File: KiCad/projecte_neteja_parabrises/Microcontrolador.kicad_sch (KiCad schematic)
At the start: 11 parts, among them J1 Conn_01x09_Pin, U1 PIC24HJ32GP302, U2 SN74LVC2T45DCUR, U3 HDC2080, Y1 Crystal

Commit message: SCH V1
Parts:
- added C1, C2: 100n, symbol Device:C
- added J2: DE9_Pins, symbol Connector:DE9_Pins
- added U1: TJA1049TK-3, Package_SON:HVSON-8-1EP_3x3mm_P0.65mm_EP1.6x2.4mm, symbol Interface_CAN_LIN:TJA1049TK-3
- J1: value Conn_01x09_Pin -> USART
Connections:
- net GATE B1 is gone; now on net SW2: U1.7 (RB3)
- net GATE B2 is gone; now on net SW3: U1.11 (RB4)
- net GATE C: now also U1.3 (RA1); no longer U1.14 (RB5)
- net GND: now also J1.4 (Pin_4), C1.2, C2.1, J2.3, U1.2 (GND), U1.9 (GND)
- net RX: now also J1.1 (Pin_1)
- net SW1: now also U1.6 (RB2); no longer U1.4 (RB0)
- net SW2: no longer U1.5 (RB1)
- net SW3: no longer U1.6 (RB2)
- net TX: now also J1.2 (Pin_2)
- net VDD: now also J1.3 (Pin_3), J2.9, U1.3 (VCC), U1.5 (VIO)
- net at U1.19 (VSS): now also C1.1
- net GATE B: now reaches U1.2 (RA0)
- net DRDY: now reaches U1.21 (RB10)
- net DRDY: now also U3.4 (DRDY)
- net CANTX: now reaches U1.22 (RP11)
- net CANTX: now also U1.1 (TXD)
- net CANRX: now reaches U1.23 (RP12)
- net CANRX: now also U1.4 (RXD)
- net at U1.8 (VSS): now also C2.2
- net RB6 renamed SW5
- net SW5: no longer U3.4 (DRDY)
- new net: J2.2, U1.6 (CANL)
- new net: J2.7, U1.7 (CANH)
- new net SW4: U1.14 (RB5)
- new net SWB: U1.5 (RB1)
- new net SWC: U1.4 (RB0)
- no-connect marks 0 -> 15
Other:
- note added: "OSCILADOR"
- note added: "SENSOR DE LLUVIA"
- note added: "USART Y BUS CAN"
- moved on the sheet: C1, C2, J1, R1, R2, R3, R4, U1, U2, U3, Y1

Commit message: UART ACABADO
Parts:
- removed J1: USART, symbol Connector:Conn_01x09_Pin
- added C5, C6, C7, C8: C, symbol Device:C
- added J3: DE9_Pins, symbol Connector:DE9_Pins
- added U7: MAX232, symbol Interface_UART:MAX232
- renumbered C1 to C3, C2 to C4, R2 to R5, R1 to R6, R3 to R7, R4 to R8, U1 to U4, U3 to U5, U2 to U6
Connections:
- net GND: now also J2.5, C7.1, C8.1, J3.5, U7.15 (GND); no longer J2.3
- net RX: now also U7.12 (R1OUT)
- net TX: now also U7.11 (T1IN)
- new net: J3.2, U7.14 (T1OUT)
- new net: J3.3, U7.13 (R1IN)
- new net: C8.2, U7.2 (VS+)
- new net: C5.1, U7.1 (C1+)
- new net: C5.2, U7.3 (C1-)
- new net: C6.1, U7.4 (C2+)
- new net: C6.2, U7.5 (C2-)
- new net: C7.2, U7.6 (VS-)
- new net VCC: U7.16 (VCC)
- no-connect marks 15 -> 22
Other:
- moved on the sheet: C1, C2, J2, U1, U4

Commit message: MICRO ACTUALIZADA
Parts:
- added C3: 100n, symbol Device:C
- added R5, R6: R, symbol Device:R
- renumbered C3 to C1, C4 to C2, C8 to C?, C6 to C?, C5 to C?, C1 to C?, C7 to C?, C2 to C?, J2 to J?, J3 to J?, R6 to R1, R5 to R2, R7 to R3, R8 to R4, U4 to U1, U6 to U2, U5 to U3, U7 to U?, U1 to U?
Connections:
- net GND: now also C3.1
- net VDD: now also R6.2
- net MCLR: now reaches U1.1 (~{MCLR})
- net MCLR: now also R5.2
- net FC1: now reaches U1.12 (RA4)
- new net: C3.2, R5.1, R6.1
- no-connect marks 22 -> 20

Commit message: ESQUEMATICO V2
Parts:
- removed C? (x4): C, symbol Device:C
- removed J? (x2): DE9_Pins, symbol Connector:DE9_Pins
- removed U?: MAX232, symbol Interface_UART:MAX232
- removed U?: TJA1049TK-3, Package_SON:HVSON-8-1EP_3x3mm_P0.65mm_EP1.6x2.4mm, symbol Interface_CAN_LIN:TJA1049TK-3
- added C17: 10p, symbol Device:C
- C3: renamed from C1; value C -> 20p
- C4: renamed from C2; value C -> 20p
- R1: renamed from R5; value R -> 470
- R2: renamed from R6; value R -> 10K
- gave numbers to parts that had none: 2
- renumbered C3 to C16, R2 to R5, R1 to R6, R3 to R7, R4 to R8, U1 to U4, U3 to U5, U2 to U6
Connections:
- net GND: now also U4.19 (VSS), U4.27 (AVSS), C17.2
- net at C1.1: now also U4.28 (AVDD); no longer U4.19 (VSS)
- net at U4.20 (VCAP): now also C17.1
- net FC2: now reaches U4.24 (RP13)
- net DRDY: no longer names the net of U5.4 (DRDY)
- net DRDY: no longer U4.21 (RB10)
- new net PWM2: U4.21 (RB10)
- no-connect marks 20 -> 1
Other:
- note added: "MICROPROCESADOR"
- note removed: "USART Y BUS CAN"
- moved on the sheet: C1, C16, C2, R1, R2, U4

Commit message: Error de nombres solucionado
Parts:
- renumbered R6 to R10, R7 to R11, R8 to R12, R1 to R7, R2 to R8, R5 to R9, U4 to U5, U5 to U6, U6 to U7
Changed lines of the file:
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@@
 		(dnp no)
 		(fields_autoplaced yes)
-		(property "Reference" "R5"
+		(property "Reference" "R9"
 			(at 234.95 48.2599 0)
 			(effects
@@
 			(project "projecte_neteja_parabrises"
 				(path "/83fe8808-b70b-463e-9fcd-89556c9690a9/7b0ed2a6-dd0e-4fb8-9a3e-b81f5336277e"
-					(reference "R5")
+					(reference "R9")
 					(unit 1)
 				)
@@
 		(dnp no)
 		(fields_autoplaced yes)
-		(property "Reference" "#PWR?"
+		(property "Reference" "#PWR0110"
 			(at 95.885 60.96 0)
 			(effects
@@
 			(project "projecte_neteja_parabrises"
 				(path "/83fe8808-b70b-463e-9fcd-89556c9690a9/7b0ed2a6-dd0e-4fb8-9a3e-b81f5336277e"
-					(reference "#PWR?")
+					(reference "#PWR0110")
 					(unit 1)
 				)
@@
 		(dnp no)
 		(fields_autoplaced yes)
-		(property "Reference" "U5"
-			(at 214.8683 36.195 0)
+		(property "Reference" "U6"
+			(at 214.8683 35.56 0)
 			(effects
 				(font
@@
 		)
 		(property "Value" "HDC2080"
-			(at 214.8683 38.735 0)
+			(at 214.8683 38.1 0)
 			(effects
 				(font
@@
 			(project "projecte_neteja_parabrises"
 				(path "/83fe8808-b70b-463e-9fcd-89556c9690a9/7b0ed2a6-dd0e-4fb8-9a3e-b81f5336277e"
-					(reference "U5")
+					(reference "U6")
 					(unit 1)
 				)
@@
 		(dnp no)
 		(fields_autoplaced yes)
-		(property "Reference" "U4"
-			(at 66.04 55.245 0)
+		(property "Reference" "U5"
+			(at 66.04 54.61 0)
 			(effects
 				(font
@@
 		)
 		(property "Value" "PIC24HJ32GP302"
-			(at 66.04 57.785 0)
+			(at 66.04 57.15 0)
 			(effects
 				(font
@@
 			(project "projecte_neteja_parabrises"
 				(path "/83fe8808-b70b-463e-9fcd-89556c9690a9/7b0ed2a6-dd0e-4fb8-9a3e-b81f5336277e"
-					(reference "U4")
+					(reference "U5")
 					(unit 1)
 				)
@@
 		(dnp no)
 		(fields_autoplaced yes)
-		(property "Reference" "#PWR?"
+		(property "Reference" "#PWR0111"
 			(at 90.805 68.58 0)
 			(effects
@@
 			(project "projecte_neteja_parabrises"
 				(path "/83fe8808-b70b-463e-9fcd-89556c9690a9/7b0ed2a6-dd0e-4fb8-9a3e-b81f5336277e"
-					(reference "#PWR?")
+					(reference "#PWR0111")
 					(unit 1)
 				)
@@
 		(dnp no)
 		(fields_autoplaced yes)
-		(property "Reference" "#PWR?"
+		(property "Reference" "#PWR0113"
 			(at 20.32 33.02 0)
 			(effects
@@
 			(project "projecte_neteja_parabrises"
 				(path "/83fe8808-b70b-463e-9fcd-89556c9690a9/7b0ed2a6-dd0e-4fb8-9a3e-b81f5336277e"
-					(reference "#PWR?")
+					(reference "#PWR0113")
 					(unit 1)
 				)
@@
 		(on_board yes)
 		(dnp no)
-		(property "Reference" "R1"
+		(property "Reference" "R7"
 			(at 38.1 31.115 90)
 			(effects
@@
 			(project "projecte_neteja_parabrises"
 				(path "/83fe8808-b70b-463e-9fcd-89556c9690a9/7b0ed2a6-dd0e-4fb8-9a3e-b81f5336277e"
-					(reference "R1")
+					(reference "R7")
 					(unit 1)
 				)
@@
 		(fields_autoplaced yes)
 		(property "Reference" "C17"
-			(at 111.76 75.565 90)
+			(at 111.76 74.93 90)
 			(effects
 				(font
@@
 		)
 		(property "Value" "10p"
-			(at 111.76 78.105 90)
+			(at 111.76 77.47 90)
 			(effects
 				(font
@@
 		(on_board yes)
 		(dnp no)
-		(property "Reference" "R2"
+		(property "Reference" "R8"
 			(at 43.18 22.225 0)
 			(effects
@@
 			(project "projecte_neteja_parabrises"
 				(path "/83fe8808-b70b-463e-9fcd-89556c9690a9/7b0ed2a6-dd0e-4fb8-9a3e-b81f5336277e"
-					(reference "R2")
+					(reference "R8")
 					(unit 1)
 				)
@@
 		(dnp no)
 		(fields_autoplaced yes)
-		(property "Reference" "#PWR?"
+		(property "Reference" "#PWR0112"
 			(at 115.57 88.9 0)
 			(effects
@@
 			(project "projecte_neteja_parabrises"
 				(path "/83fe8808-b70b-463e-9fcd-89556c9690a9/7b0ed2a6-dd0e-4fb8-9a3e-b81f5336277e"
-					(reference "#PWR?")
+					(reference "#PWR0112")
 					(unit 1)
 				)
@@
 		(dnp no)
 		(fields_autoplaced yes)
-		(property "Reference" "R6"
+		(property "Reference" "R10"
 			(at 236.22 33.6549 0)
 			(effects
@@
 			(project "projecte_neteja_parabrises"
 				(path "/83fe8808-b70b-463e-9fcd-89556c9690a9/7b0ed2a6-dd0e-4fb8-9a3e-b81f5336277e"
-					(reference "R6")
+					(reference "R10")
 					(unit 1)
 				)
@@
 		(dnp no)
 		(fields_autoplaced yes)
-		(property "Reference" "R8"
+		(property "Reference" "R12"
 			(at 269.24 46.3549 0)
 			(effects
@@
 			(project "projecte_neteja_parabrises"
 				(path "/83fe8808-b70b-463e-9fcd-89556c9690a9/7b0ed2a6-dd0e-4fb8-9a3e-b81f5336277e"
-					(reference "R8")
+					(reference "R12")
 					(unit 1)
 				)
@@
 		(dnp no)
 		(fields_autoplaced yes)
-		(property "Reference" "R7"
+		(property "Reference" "R11"
 			(at 269.24 33.6549 0)
 			(effects
@@
 			(project "projecte_neteja_parabrises"
 				(path "/83fe8808-b70b-463e-9fcd-89556c9690a9/7b0ed2a6-dd0e-4fb8-9a3e-b81f5336277e"
-					(reference "R7")
+					(reference "R11")
 					(unit 1)
 				)
@@
 		(dnp no)
 		(fields_autoplaced yes)
-		(property "Reference" "U6"
+		(property "Reference" "U7"
 			(at 254.8733 53.34 0)
 			(effects
@@
 			(project "projecte_neteja_parabrises"
 				(path "/83fe8808-b70b-463e-9fcd-89556c9690a9/7b0ed2a6-dd0e-4fb8-9a3e-b81f5336277e"
-					(reference "U6")
-					(unit 1)
-				)
+					(reference "U7")
+					(unit 1)
+				)

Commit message: huellas
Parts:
- C1, C16, C17, C2, C3, C4: footprint (none) -> Capacitor_SMD:C_0805_2012Metric
- R10, R11, R12, R7, R8, R9: footprint (none) -> Resistor_SMD:R_0603_1608Metric_Pad0.98x0.95mm_HandSolder
- Y1: footprint (none) -> Crystal:Crystal_SMD_HC49-SD
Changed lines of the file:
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@@
 			)
 		)
-		(property "Footprint" ""
+		(property "Footprint" "Resistor_SMD:R_0603_1608Metric_Pad0.98x0.95mm_HandSolder"
 			(at 231.267 49.53 90)
 			(effects
@@
 			)
 		)
-		(property "Footprint" ""
+		(property "Footprint" "Capacitor_SMD:C_0805_2012Metric"
 			(at 33.02 25.7048 0)
 			(effects
@@
 			)
 		)
-		(property "Footprint" ""
+		(property "Footprint" "Capacitor_SMD:C_0805_2012Metric"
 			(at 169.2402 49.53 0)
 			(effects
@@
 			)
 		)
-		(property "Footprint" ""
+		(property "Footprint" "Capacitor_SMD:C_0805_2012Metric"
 			(at 83.4898 54.61 0)
 			(effects
@@
 			)
 		)
-		(property "Footprint" ""
+		(property "Footprint" "Resistor_SMD:R_0603_1608Metric_Pad0.98x0.95mm_HandSolder"
 			(at 33.782 30.48 90)
 			(effects
@@
 			)
 		)
-		(property "Footprint" ""
+		(property "Footprint" "Crystal:Crystal_SMD_HC49-SD"
 			(at 160.655 39.37 0)
 			(effects
@@
 			)
 		)
-		(property "Footprint" ""
+		(property "Footprint" "Capacitor_SMD:C_0805_2012Metric"
 			(at 154.0002 49.53 0)
 			(effects
@@
 			)
 		)
-		(property "Footprint" ""
+		(property "Footprint" "Capacitor_SMD:C_0805_2012Metric"
 			(at 115.57 81.5848 0)
 			(effects
@@
 			)
 		)
-		(property "Footprint" ""
+		(property "Footprint" "Resistor_SMD:R_0603_1608Metric_Pad0.98x0.95mm_HandSolder"
 			(at 41.91 28.448 90)
 			(effects
@@
 			)
 		)
-		(property "Footprint" ""
+		(property "Footprint" "Resistor_SMD:R_0603_1608Metric_Pad0.98x0.95mm_HandSolder"
 			(at 232.537 34.925 90)
 			(effects
@@
 			)
 		)
-		(property "Footprint" ""
+		(property "Footprint" "Resistor_SMD:R_0603_1608Metric_Pad0.98x0.95mm_HandSolder"
 			(at 264.922 47.625 90)
 			(effects
@@
 			)
 		)
-		(property "Footprint" ""
+		(property "Footprint" "Resistor_SMD:R_0603_1608Metric_Pad0.98x0.95mm_HandSolder"
 			(at 264.922 34.925 90)
 			(effects
@@
 			)
 		)
-		(property "Footprint" ""
+		(property "Footprint" "Capacitor_SMD:C_0805_2012Metric"
 			(at 36.83 79.6798 0)
 			(effects

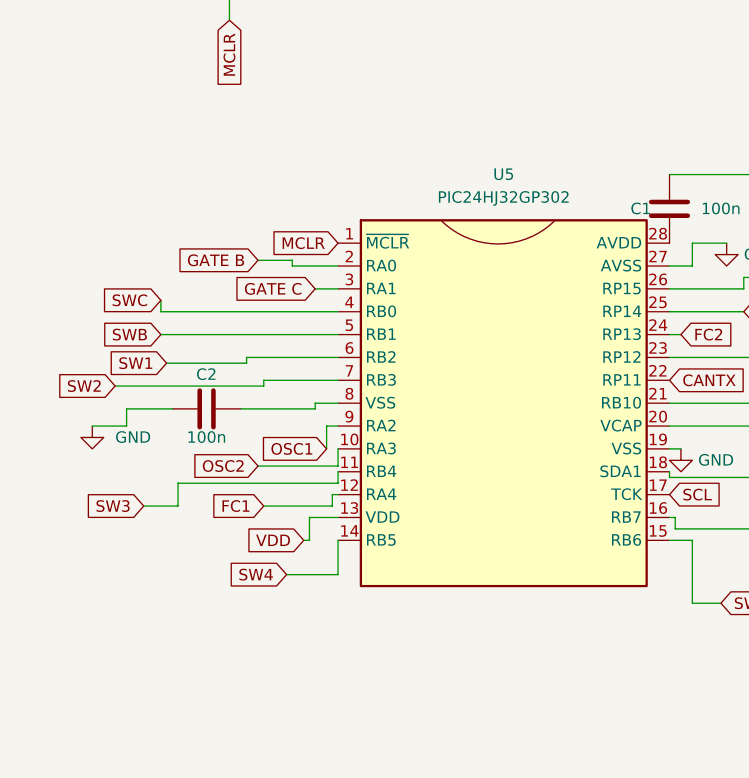
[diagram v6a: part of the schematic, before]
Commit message: Actualización huellas
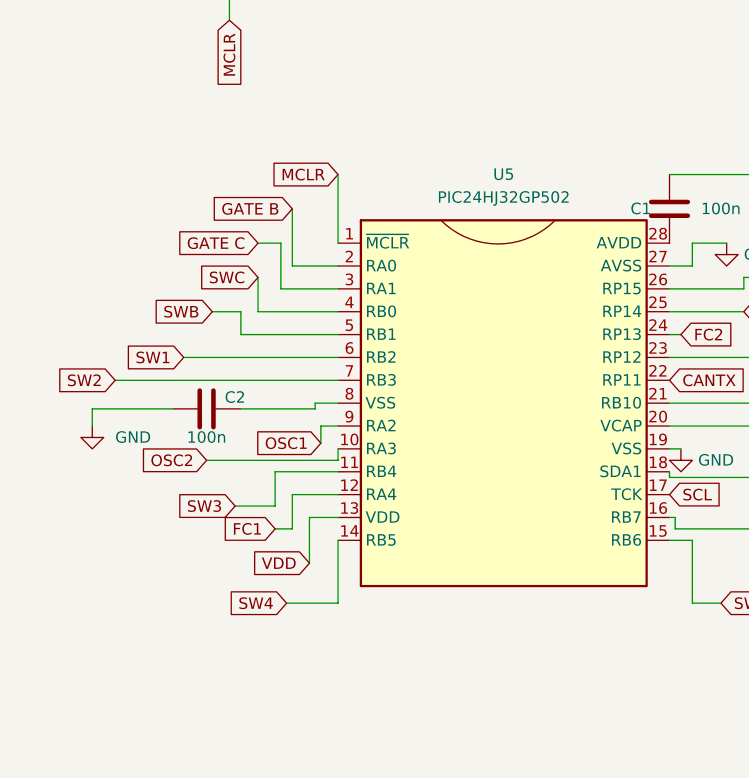
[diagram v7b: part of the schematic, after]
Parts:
- U5: value PIC24HJ32GP302 -> PIC24HJ32GP502; footprint (none) -> Package_SO:SOIC-28W_7.5x17.9mm_P1.27mm

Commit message: botonera
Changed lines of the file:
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@@
+	(wire
+		(pts
+			(xy 48.26 26.67) (xy 45.72 26.67)
+		)
+		(stroke
+			(width 0)
+			(type default)
+		)
+	)
 	(wire
 		(pts
@@
 	(global_label "VDD"
 		(shape input)
-		(at 45.72 26.67 0)
+		(at 48.26 26.67 0)
 		(fields_autoplaced yes)
 		(effects
@@
 		)
 		(property "Intersheetrefs" "${INTERSHEET_REFS}"
-			(at 52.3338 26.67 0)
+			(at 54.8738 26.67 0)
 			(effects
 				(font
